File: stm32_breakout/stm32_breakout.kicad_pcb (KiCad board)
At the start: 2 copper layers, 27.4 x 25 mm, 16 parts, among them U6 STM32F103RETx

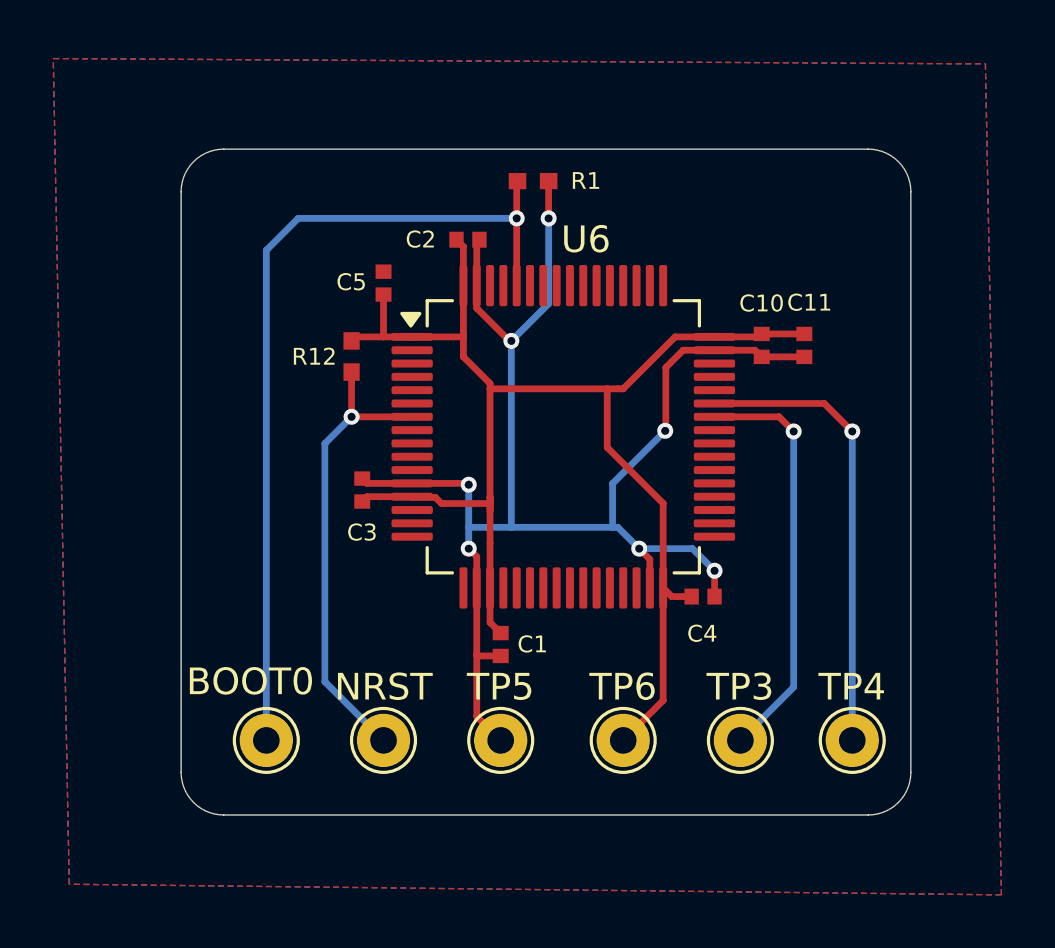
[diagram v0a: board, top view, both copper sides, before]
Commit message: Included resistors for EN/GPIO0 on ESP32
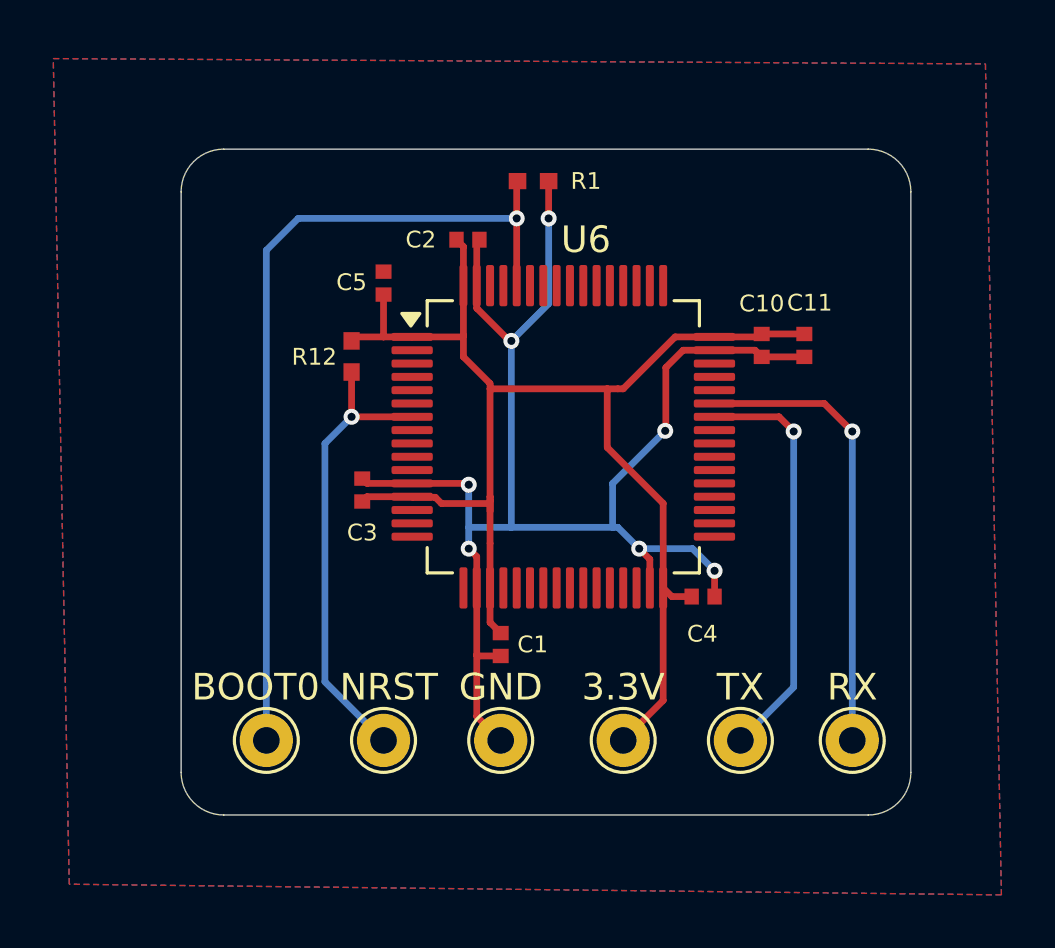
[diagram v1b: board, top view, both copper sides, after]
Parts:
- renumbered TP6 to 3.3V, TP5 to GND, TP4 to RX, TP3 to TX
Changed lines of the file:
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@@
 		(descr "THT pad as test Point, diameter 2.0mm, hole diameter 1.0mm")
 		(tags "test point THT pad")
-		(property "Reference" "TP6"
+		(property "Reference" "3.3V"
 			(at 0 -1.998 0)
 			(layer "F.SilkS")
@@
 		(tags "test point THT pad")
 		(property "Reference" "NRST"
-			(at 0 -1.998 0)
+			(at 0.2 -1.998 0)
 			(layer "F.SilkS")
 			(effects
@@
 		(descr "THT pad as test Point, diameter 2.0mm, hole diameter 1.0mm")
 		(tags "test point THT pad")
-		(property "Reference" "TP4"
+		(property "Reference" "RX"
 			(at 0 -1.998 0)
 			(layer "F.SilkS")
@@
 		(descr "THT pad as test Point, diameter 2.0mm, hole diameter 1.0mm")
 		(tags "test point THT pad")
-		(property "Reference" "TP5"
+		(property "Reference" "GND"
 			(at 0 -1.998 0)
 			(layer "F.SilkS")
@@
 		(descr "THT pad as test Point, diameter 2.0mm, hole diameter 1.0mm")
 		(tags "test point THT pad")
-		(property "Reference" "TP3"
+		(property "Reference" "TX"
 			(at 0 -1.998 0)
 			(layer "F.SilkS")
@@
 		(tags "test point THT pad")
 		(property "Reference" "BOOT0"
-			(at -0.6 -2.2 0)
-			(layer "F.SilkS")
-			(effects
+			(at -0.4 -2 0)
+			(layer "F.SilkS")
+			(effects

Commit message: Added silkscreen to boards
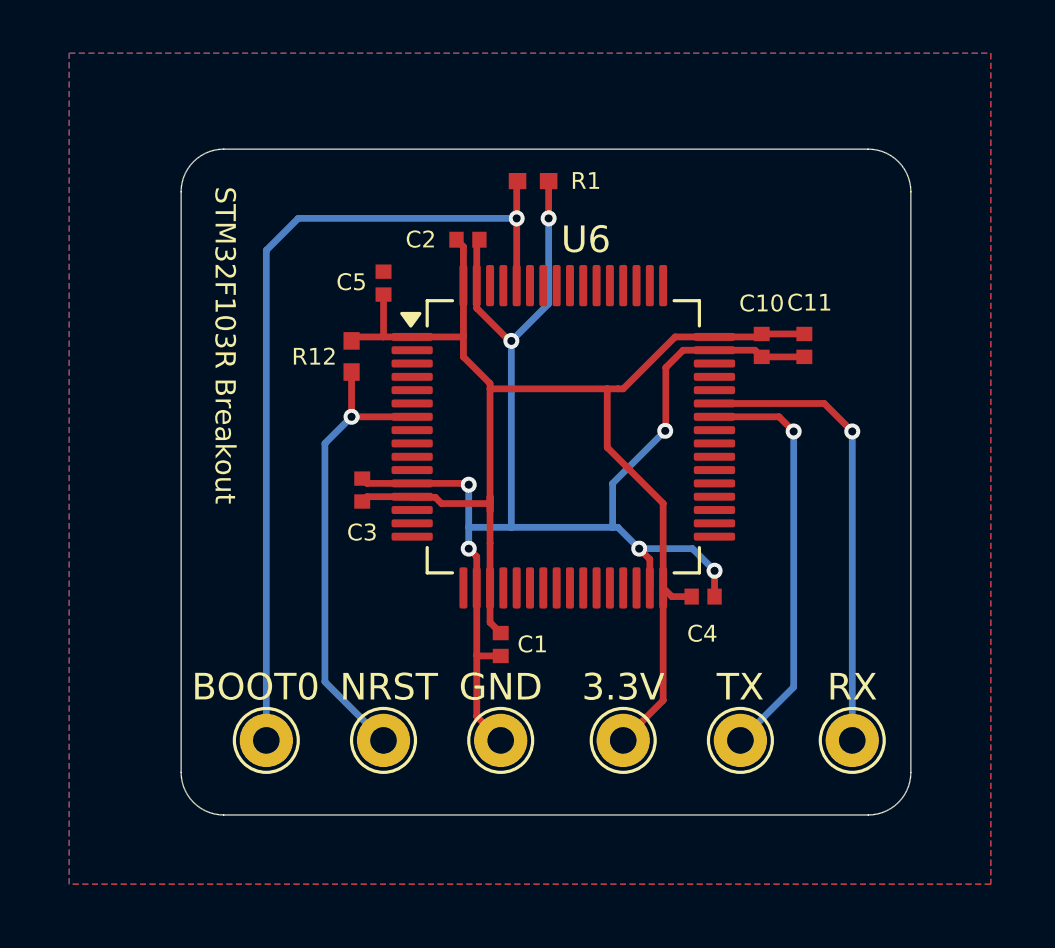
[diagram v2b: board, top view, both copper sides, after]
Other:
- board text added: "STM32F103R Breakout"
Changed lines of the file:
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@@
 		(layer "Edge.Cuts")
+	)
+	(gr_text "STM32F103R Breakout\n"
+		(at 111.2 50.2 270)
+		(layer "F.SilkS")
+		(effects
+			(font
+				(size 0.762 0.762)
+				(thickness 0.15)
+			)
+			(justify left bottom)
+		)
 	)
 	(segment
@@
 		(polygon
 			(pts
-				(xy 105.2 45.4) (xy 140.2 45.6) (xy 140.8 76.8) (xy 105.8 76.4)
+				(xy 105.8 45.2) (xy 140.4 45.2) (xy 140.4 76.4) (xy 105.8 76.4)
 			)
 		)
